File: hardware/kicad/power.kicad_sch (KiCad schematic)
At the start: 21 parts, among them Q2 FS8205A, U1 TC4056A, U2 DW01A, U3 MT3608, U9 MT3608

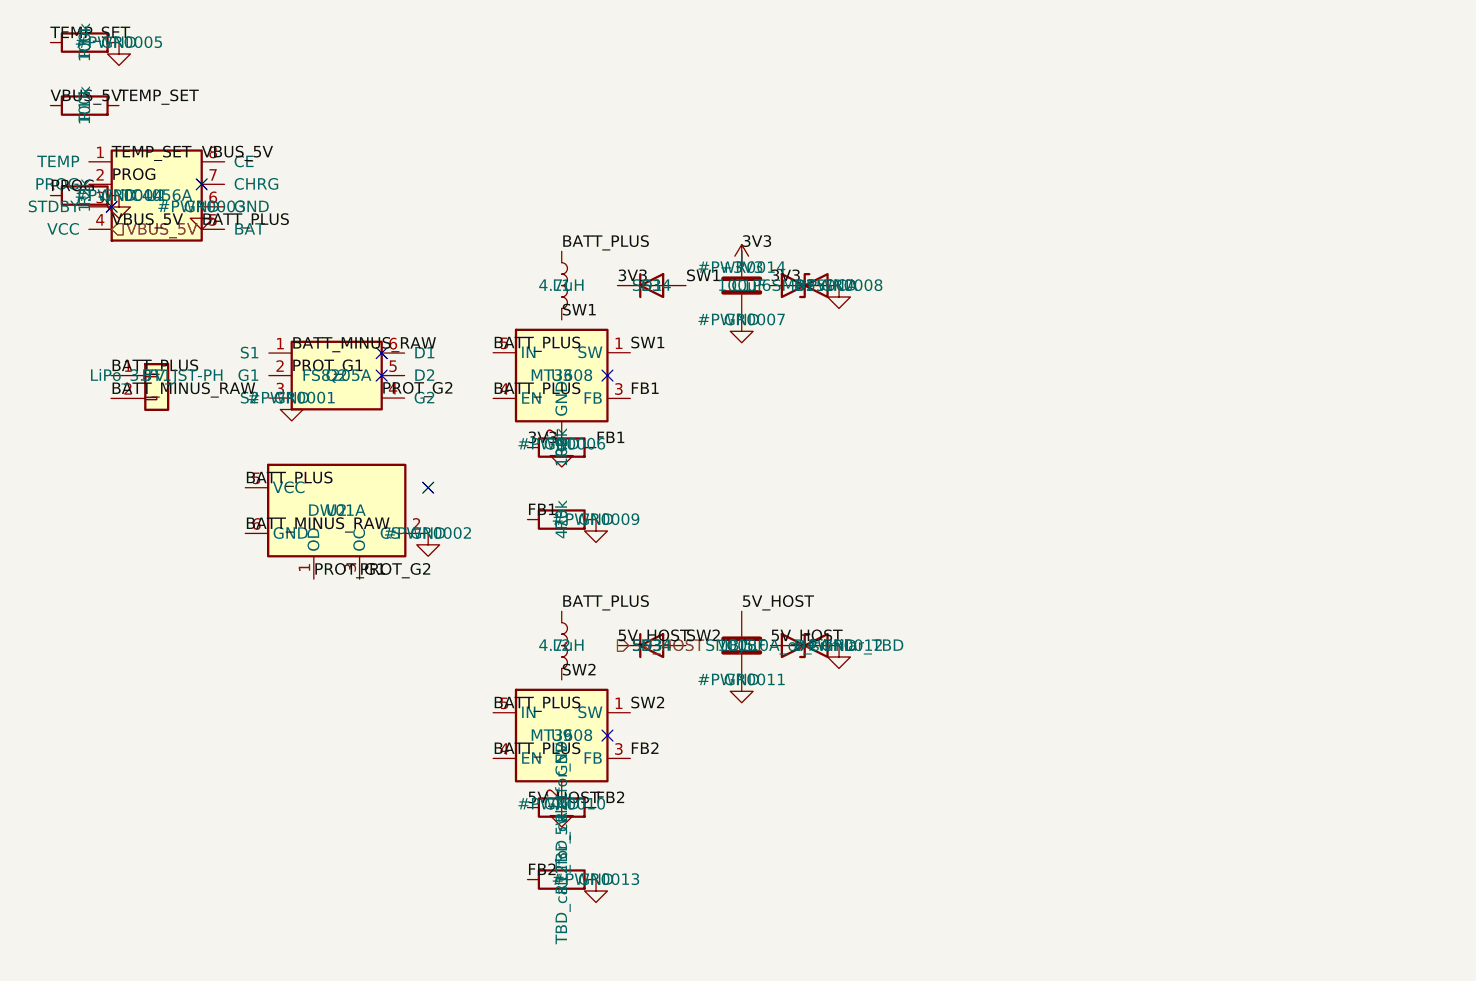
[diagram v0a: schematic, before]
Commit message: fix: repair schematic connectivity, real MAX3421E pinout, footprint assignment
- Root sheet pins were placed outside the sheet boxes, so no cross-sheet
  net (IO5->CI-V, USB D+/D-, SPI, VBUS_5V, 5V_HOST) was actually connected.
  Rebuilt pins on the sheet borders with wire stubs + labels.
- MCU: SW1/SW2 pin 2 carried both GND and EN/BOOT0 (short to ground);
  GND moved to pin 1. Unused ESP32 GPIOs marked no-connect.
- USB_Host rebuilt around the real MAX3421E TQFN-32 pinout (datasheet
  19-3953): 33 ohm D+/D- series resistors, 1uF VCC/VBCOMP, 0.1uF VL.
- J1 now AudioJack3 (T/R/S) with CUI SJ1-3523N footprint; Q1 is a real
  2N7000 (TO-92).
- PWR_FLAGs added; ERC (raw kicad-cli) has 0 errors.
- Board outline 65x45 mm, 54 footprints assigned and written to symbol
  Footprint fields, netlist applied. Placement is a rough grid only; no
  routing yet.
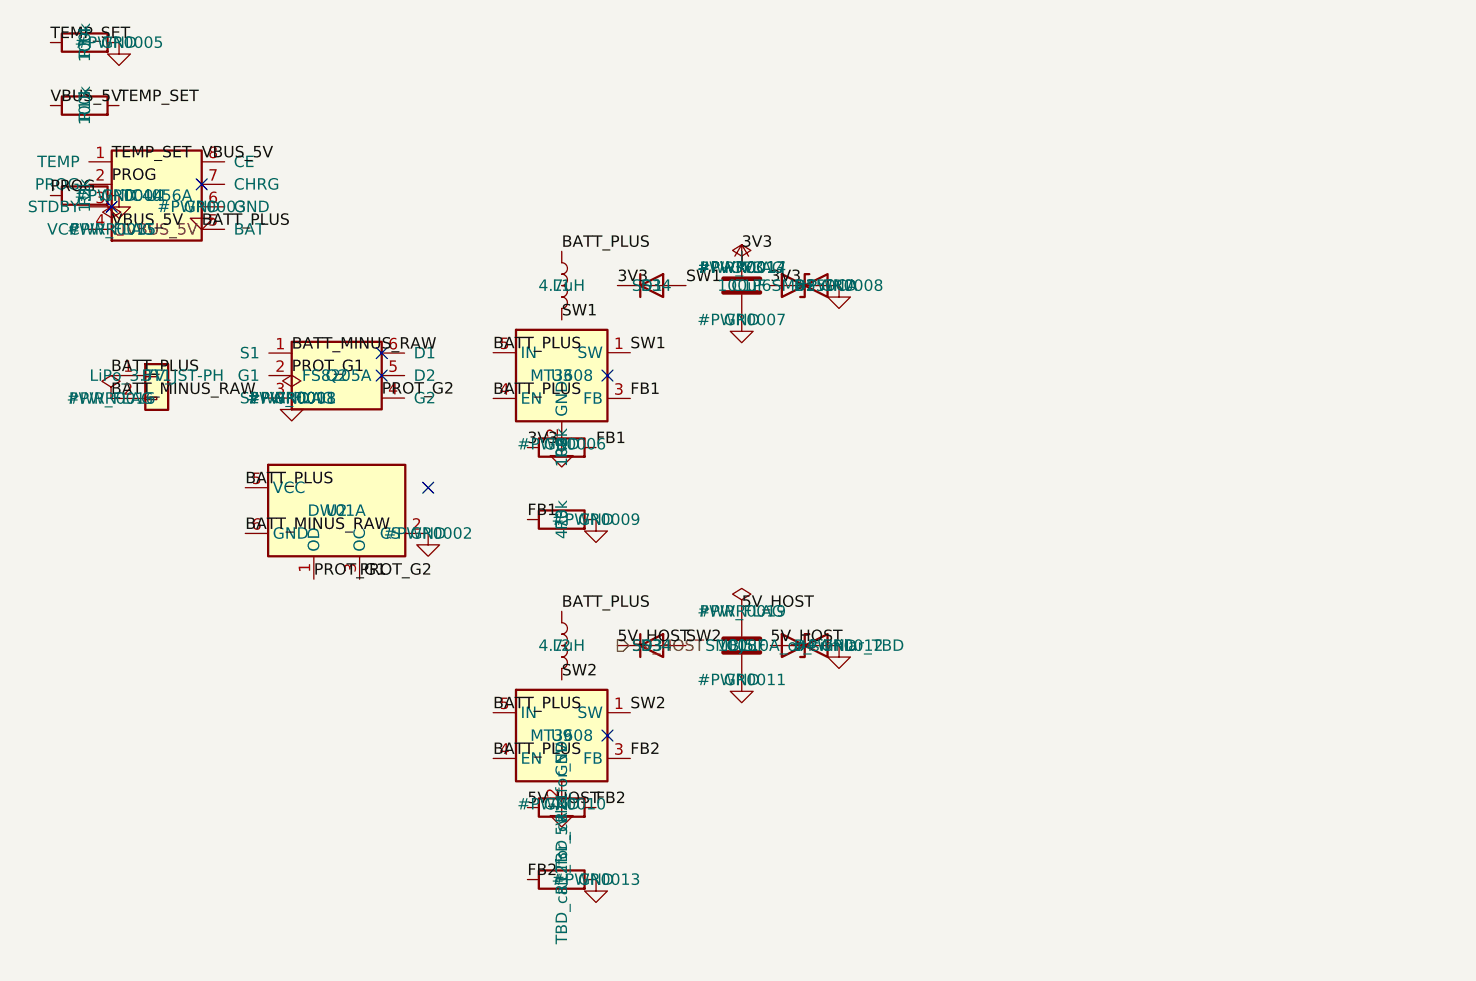
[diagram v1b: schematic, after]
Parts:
- BT1: footprint (none) -> Connector_JST:JST_PH_B2B-PH-K_1x02_P2.00mm_Vertical
- C1, C18: footprint (none) -> Capacitor_SMD:C_1206_3216Metric
- D1, D3: footprint (none) -> Diode_SMD:D_SMA
- D2, D4: footprint (none) -> Diode_SMD:D_SMB
- L1, L2: footprint (none) -> Inductor_SMD:L_6.3x6.3_H3
- R1, R11, R12, R13, R14, R2, R3: footprint (none) -> Resistor_SMD:R_0603_1608Metric

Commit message: fix: datasheet audit - correct charger pinout, LDO for 3V3, DW01A/FS8205A, MAX3232, CI-V RX
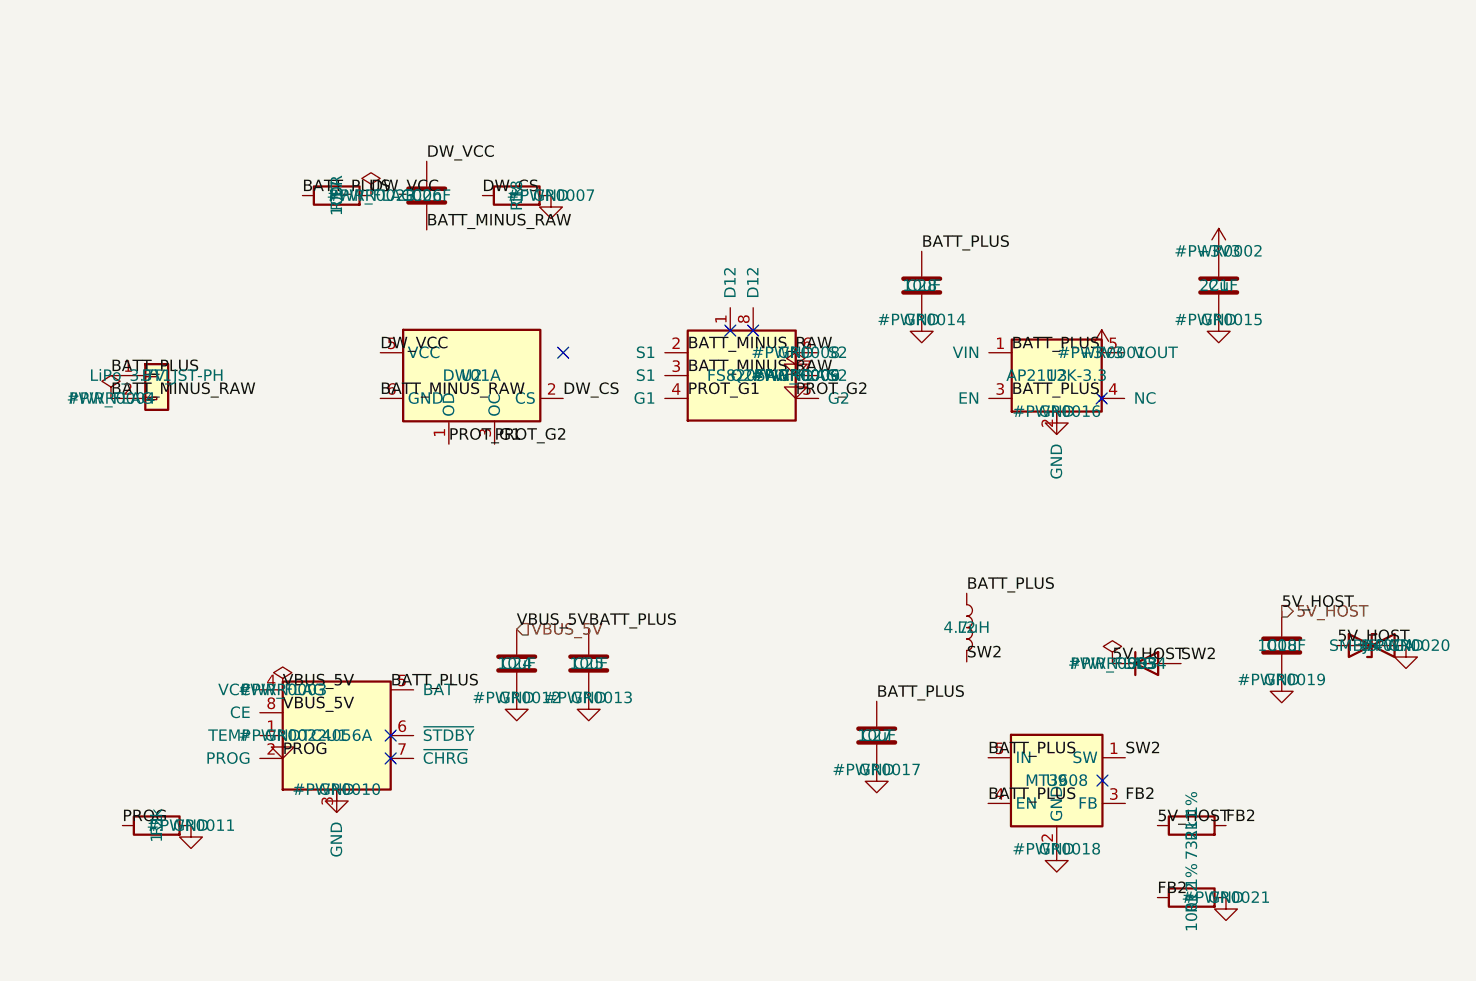
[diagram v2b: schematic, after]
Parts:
- removed D1: SS34, Diode_SMD:D_SMA, symbol Device:D
- removed D2: P6SMB550CA, Diode_SMD:D_SMB, symbol Device:D_TVS
- removed L1: 4.7uH, Inductor_SMD:L_6.3x6.3_H3, symbol Device:L
- removed Q2: FS8205A, Package_TO_SOT_SMD:SOT-23-6, symbol WaveRig_Custom:FS8205A
- removed R13, R14, R2: 100k, Resistor_SMD:R_0603_1608Metric, symbol Device:R
- removed R3: 470k, Resistor_SMD:R_0603_1608Metric, symbol Device:R
- removed U1: TC4056A, Package_SO:SOIC-8_3.9x4.9mm_P1.27mm, symbol WaveRig_Custom:TC4056A
- removed U3: MT3608, Package_TO_SOT_SMD:SOT-23-6, symbol Regulator_Switching:MT3608
- added C24, C25, C27, C28: 10uF, Capacitor_SMD:C_0805_2012Metric, symbol Device:C
- added C26: 100nF, Capacitor_SMD:C_0603_1608Metric, symbol Device:C
- added Q2: FS8205A, Package_SO:TSSOP-8_4.4x3mm_P0.65mm, symbol WaveRig_Custom:FS8205A_TSSOP8
- added R17: 100R, Resistor_SMD:R_0603_1608Metric, symbol Device:R
- added R18: 1k, Resistor_SMD:R_0603_1608Metric, symbol Device:R
- added U1: TC4056A, Package_SO:SOIC-8_3.9x4.9mm_P1.27mm, symbol WaveRig_Custom:TC4056A_SOP8
- added U3: AP2112K-3.3, Package_TO_SOT_SMD:SOT-23-5, symbol WaveRig_Custom:AP2112K-3.3
- C1: value 100uF -> 22uF; footprint Capacitor_SMD:C_1206_3216Metric -> Capacitor_SMD:C_0805_2012Metric
- D4: value SMBJ5.0A_or_similar_TBD -> SMBJ5.0CA
- R11: value TBD_calc_for_5V -> 732k 1%
- R12: value TBD_calc_for_5V -> 100k 1%
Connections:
- net +3V3: now also U3.5 (VOUT)
- net BATT_MINUS_RAW: now also C26.2, Q2.2 (S1), Q2.3 (S1)
- net BATT_PLUS: now also C25.1, C27.1, C28.1, R17.1, U1.5 (BAT), U3.1 (VIN), U3.3 (EN); no longer U2.5 (VCC)
- net GND: now also C24.2, C25.2, C27.2, C28.2, Q2.6 (S2), Q2.7 (S2), R18.2, U1.1 (TEMP), U1.3 (GND), U3.2 (GND); no longer U2.2 (CS)
- net PROG: now also U1.2 (PROG)
- net PROT_G1: now also Q2.4 (G1)
- net PROT_G2: now also Q2.5 (G2)
- net VBUS_5V: now also C24.1, U1.4 (VCC), U1.8 (CE)
- new net DW_CS: R18.1, U2.2 (CS)
- new net DW_VCC: C26.1, R17.2, U2.5 (VCC)
